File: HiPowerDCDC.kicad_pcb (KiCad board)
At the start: 2 copper layers, 111.2 x 100 mm, 61 parts, among them J1 Conn_01x01, J2 Conn_01x01, J3 Conn_01x01, J4 Conn_01x01, J5 Conn_01x04, Q1 WMJ38N60, Q2 WMJ38N60, SW1 SW_Push, SW2 SW_Push, U1 ESP32-WROOM-32U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

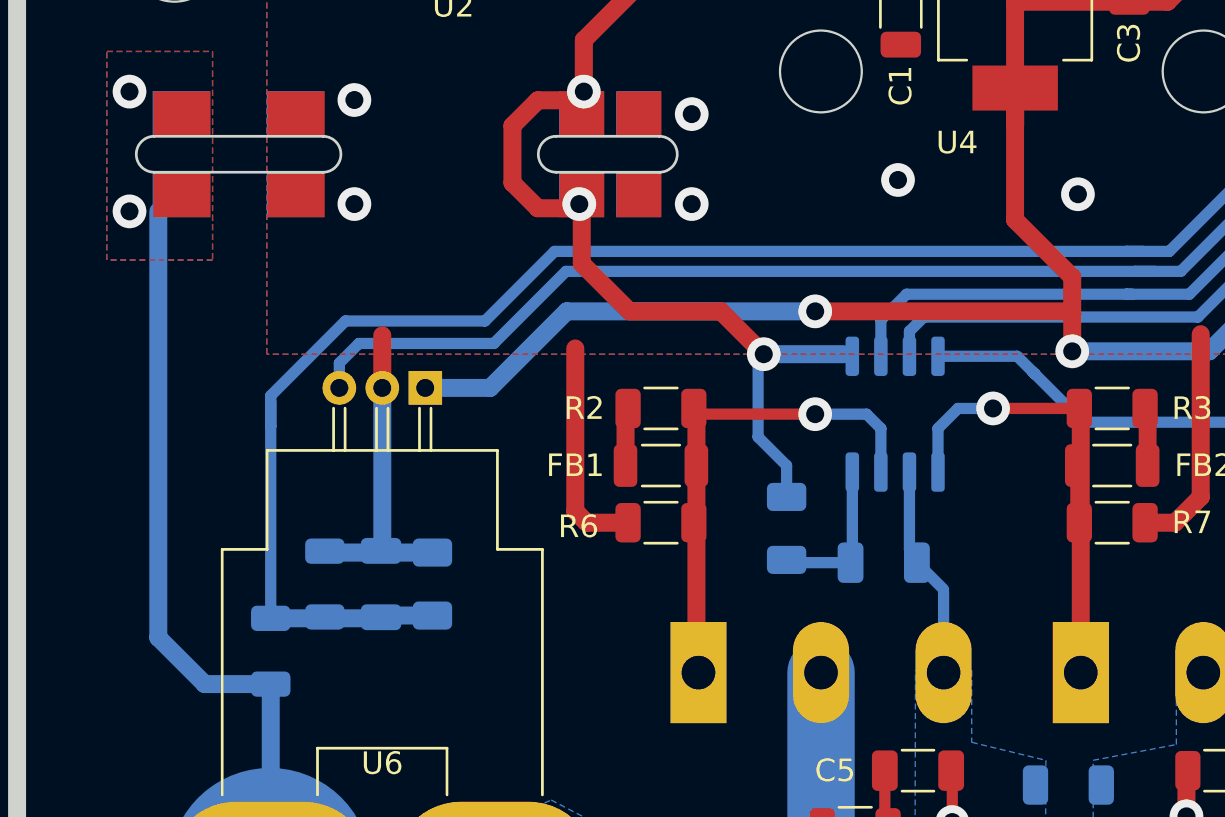
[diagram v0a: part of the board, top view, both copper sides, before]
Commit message: Changed FR107 footprint
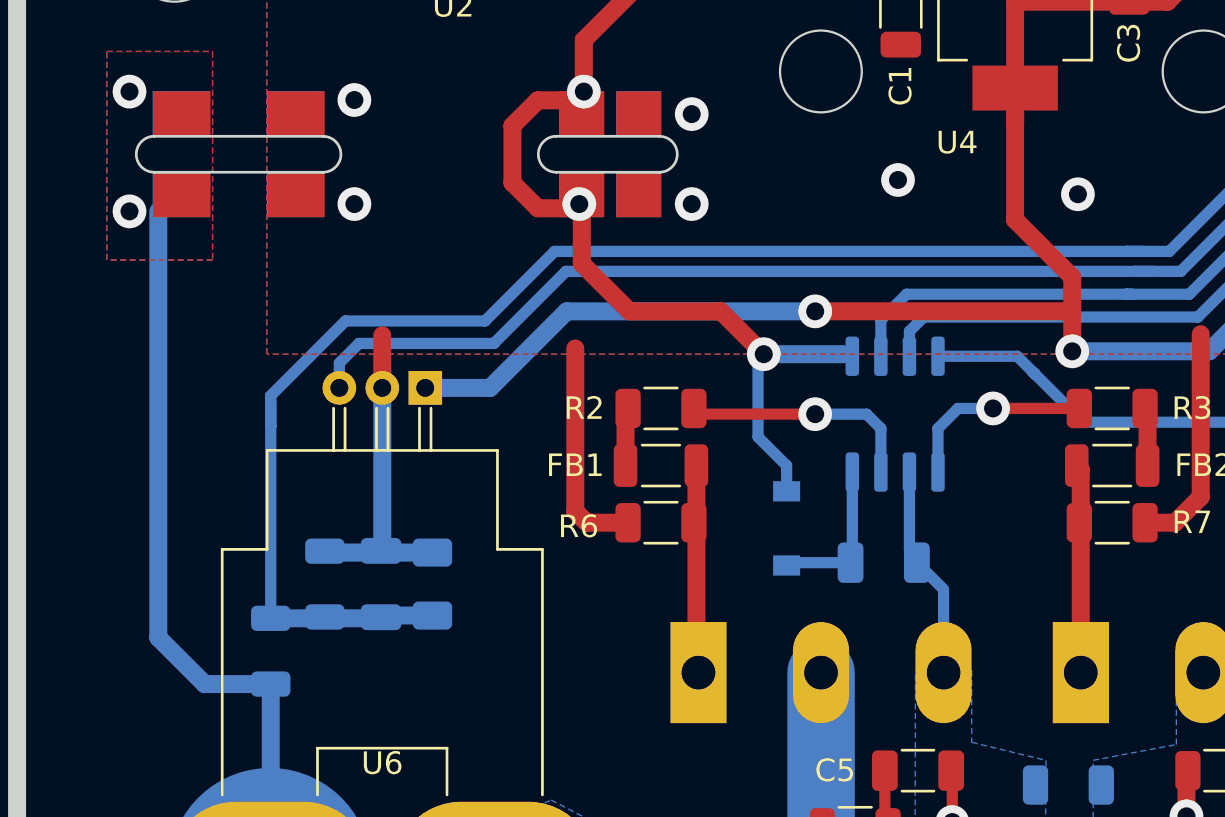
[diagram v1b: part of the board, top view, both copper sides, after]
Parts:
- D1: value D -> FR107; footprint Diode_SMD:D_1206_3216Metric -> Diode_SMD:D_SOD-123
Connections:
- R2 pad 1: Net-(FB1-Pad2) -> Net-(R2-Pad1)
- R3 pad 1: Net-(FB2-Pad2) -> Net-(R3-Pad1)
- U3 pad 5: Net-(FB2-Pad2) -> Net-(R3-Pad1)
- U3 pad 7: Net-(FB1-Pad2) -> Net-(R2-Pad1)
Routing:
- net Net-(FB2-Pad2): track 21.8 -> 9.37 mm, vias 1 -> 0
- net Net-(FB1-Pad2): track 19.8 -> 9.14 mm, vias 1 -> 0
- net Net-(R2-Pad1): track 0.00 -> 10.6 mm, vias 0 -> 1
- net Net-(R3-Pad1): track 0.00 -> 8.59 mm, vias 0 -> 1

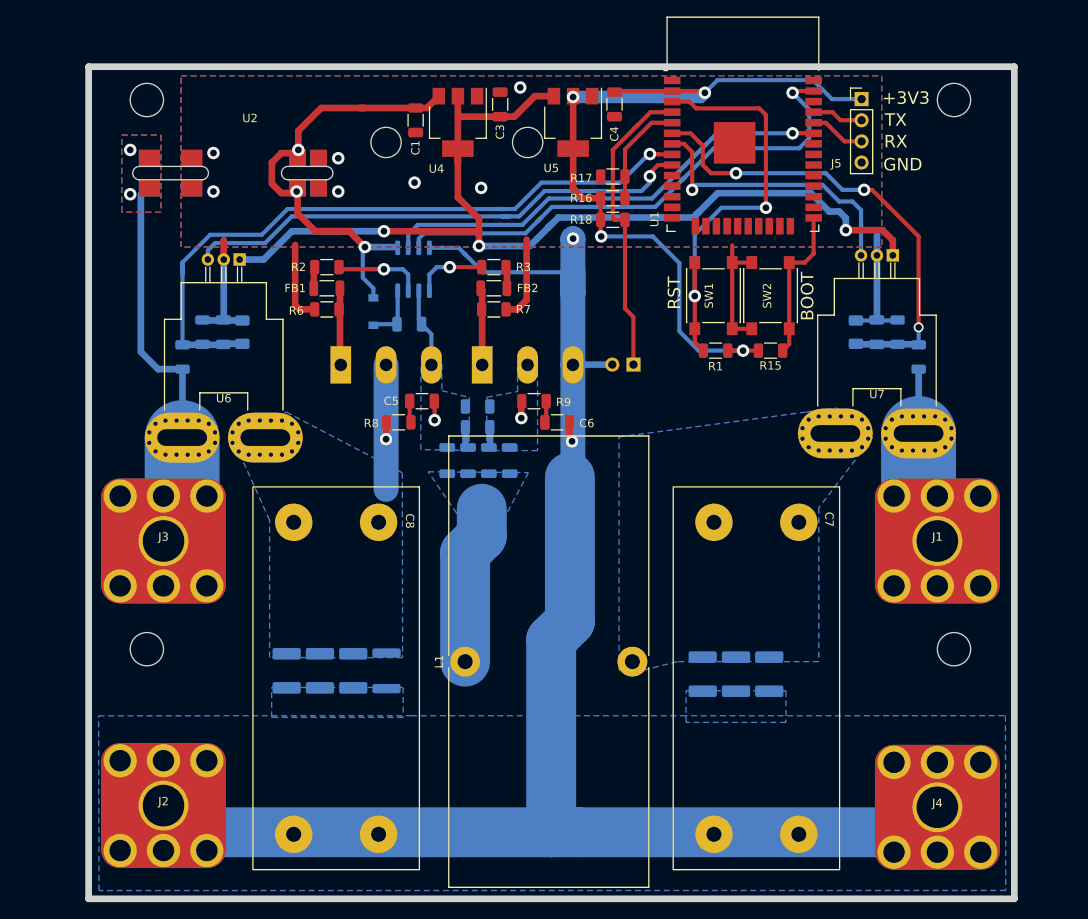
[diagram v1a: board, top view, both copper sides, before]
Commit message: Increased PCB width and made high P component more spaceous
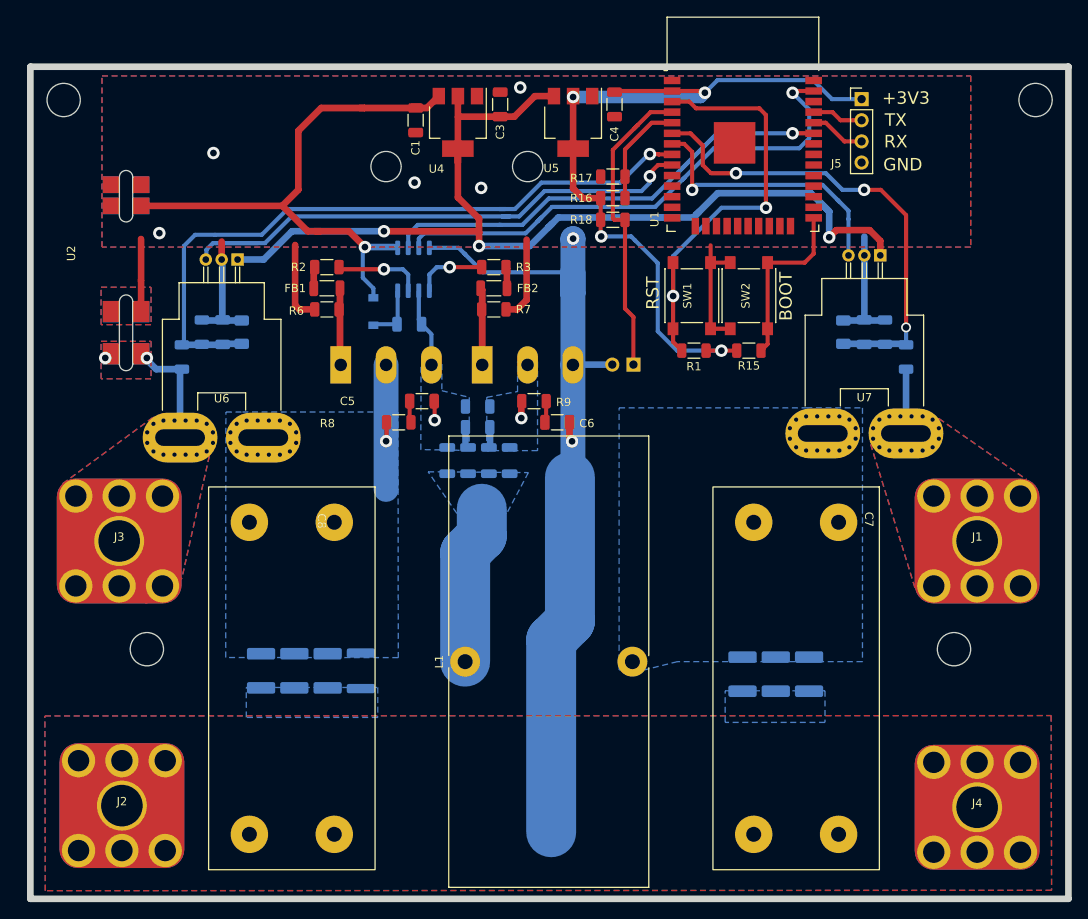
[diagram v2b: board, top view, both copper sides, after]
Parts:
- moved U2 17.7 mm to (111.2, 75.4), turned to -90 degrees
- moved C8 5.33 mm to (131.2, 126.5)
- moved J3 5.33 mm to (110.4, 110.0)
- moved J2 5.00 mm to (110.8, 141.8)
- moved C11 4.78 mm to (193.3, 126.0)
- moved C13 4.78 mm to (185.3, 126.0)
- moved C7 4.78 mm to (191.8, 126.5)
- moved C9 4.78 mm to (189.3, 126.0)
- moved J1 4.78 mm to (213.5, 110.0)
- moved J4 4.78 mm to (213.5, 142.0)
- moved C14 3.08 mm to (127.5, 125.6)
- moved C10 3.08 mm to (135.5, 125.6)
- moved C12 3.08 mm to (131.5, 125.6)
- moved R10 3.08 mm to (139.5, 125.6)
- moved SW1 2.60 mm to (179.2, 80.5)
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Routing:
- net GND: track 254.0 -> 173.4 mm, vias 9 -> 7
- net VDC: track 65.8 -> 14.0 mm
- net Net-(J1-Pad1): track 36.0 -> 12.9 mm
- net +12V: track 53.9 -> 68.5 mm, vias 3 -> 1
- net CIN: track 62.7 -> 68.1 mm
- net +3V3: track 98.2 -> 95.6 mm
- net Net-(R15-Pad1): track 18.6 -> 21.2 mm
- net COUT: track 35.7 -> 33.5 mm
- net +5V: track 123.1 -> 125.1 mm
- net Net-(R1-Pad1): track 51.4 -> 52.5 mm
- added copper zone on B.Cu, net Net-(J1-Pad1)
- added copper zone on F.Cu, net Net-(J1-Pad1)
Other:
- board size 111.2 x 100 mm -> 124.8 x 100 mm

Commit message: Added DCDC converter 12V->5V
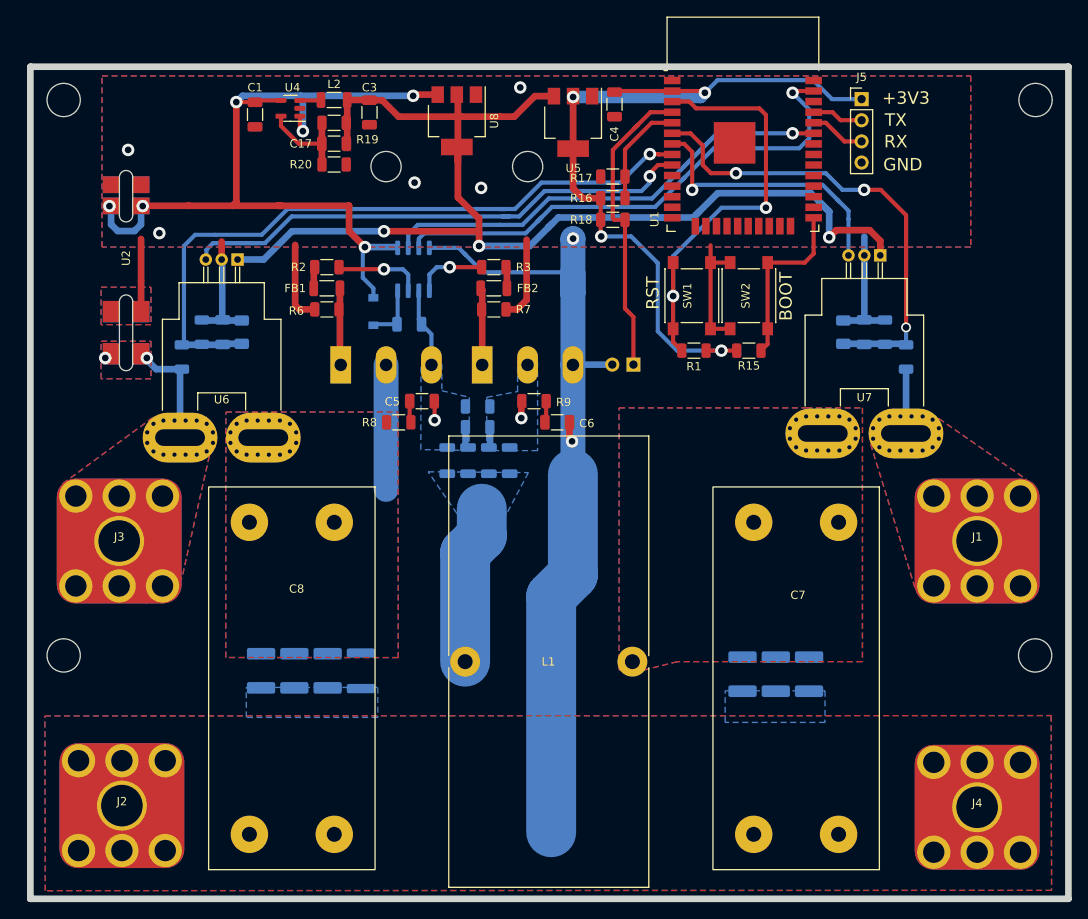
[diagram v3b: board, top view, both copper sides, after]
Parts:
- added C17: 22p, Capacitor_SMD:C_1206_3216Metric, F.Cu at (136.2, 62.2)
- added L2: 2u7, Inductor_SMD:L_1206_3216Metric, F.Cu at (136.2, 57.0)
- added R19: 4k7 1%, Resistor_SMD:R_1206_3216Metric, F.Cu at (136.2, 59.8)
- added R20: 1k 1%, Resistor_SMD:R_1206_3216Metric, F.Cu at (136.2, 64.8)
- added U8: AMS1117-5.0, Package_TO_SOT_SMD:SOT-223-3_TabPin2, F.Cu at (151.0, 59.5)
- C2: value 1u -> 10u
- U4: value AMS1117-5.0 -> XT3410; footprint Package_TO_SOT_SMD:SOT-223-3_TabPin2 -> Package_TO_SOT_SMD:SOT-23-5
- moved U4 20.2 mm to (131.0, 58.0), turned to 180 degrees
- moved C1 19.3 mm to (126.8, 58.8)
- moved C3 15.7 mm to (140.5, 58.5), turned to -90 degrees
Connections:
- U4 pad 1: GND -> +12V
- U4 pad 2: +5V -> GND
- U4 pad 3: +12V -> Net-(L2-Pad1)
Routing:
- net +12V: track 68.5 -> 99.0 mm, vias 1 -> 6
- net +5V: track 125.1 -> 144.9 mm
- net Net-(C17-Pad2): track 0.00 -> 12.0 mm
- net Net-(L2-Pad1): track 0.00 -> 2.56 mm
- net VCC: track 17.3 -> 15.0 mm, vias 1 -> 0
- added copper zone on F.Cu, net Net-(C11-Pad1)
- added copper zone on F.Cu, net VCC
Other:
- outline, holes or cut-outs redrawn

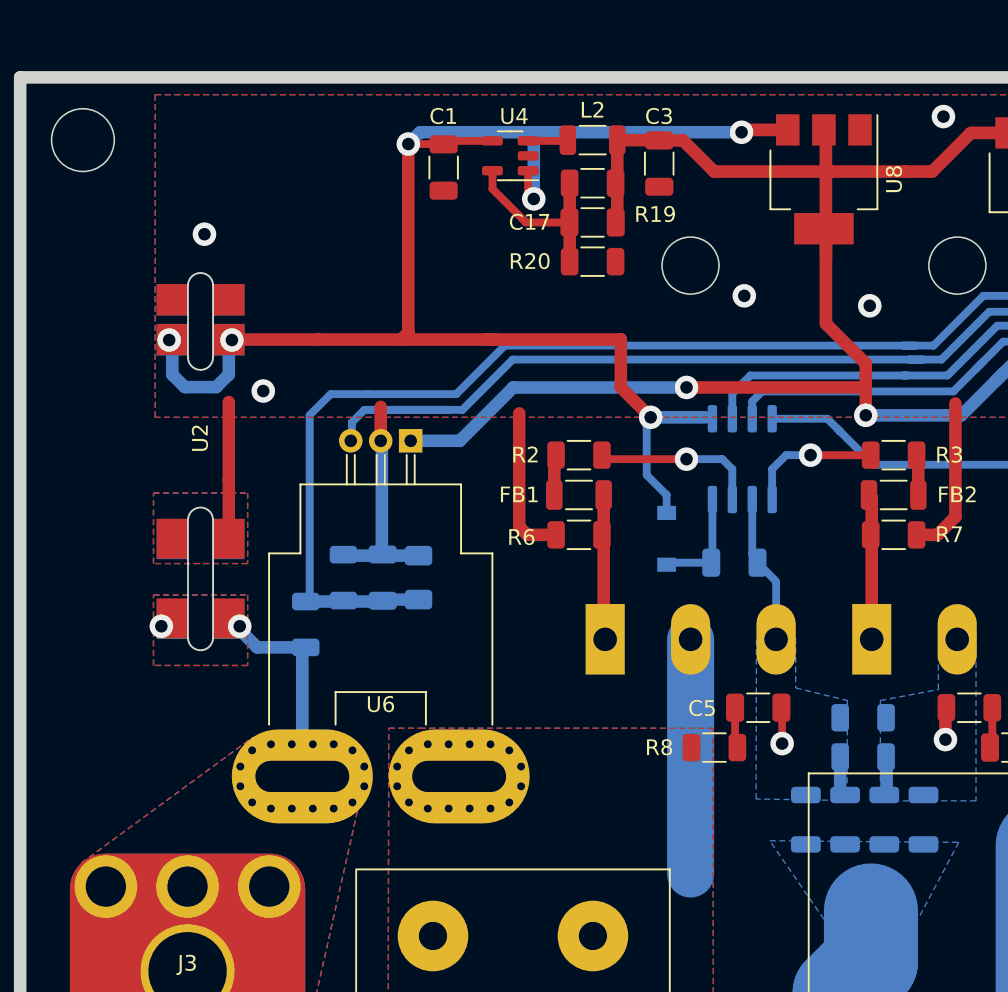
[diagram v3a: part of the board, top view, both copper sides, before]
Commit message: Changed ACDC converter to HLK-PM12
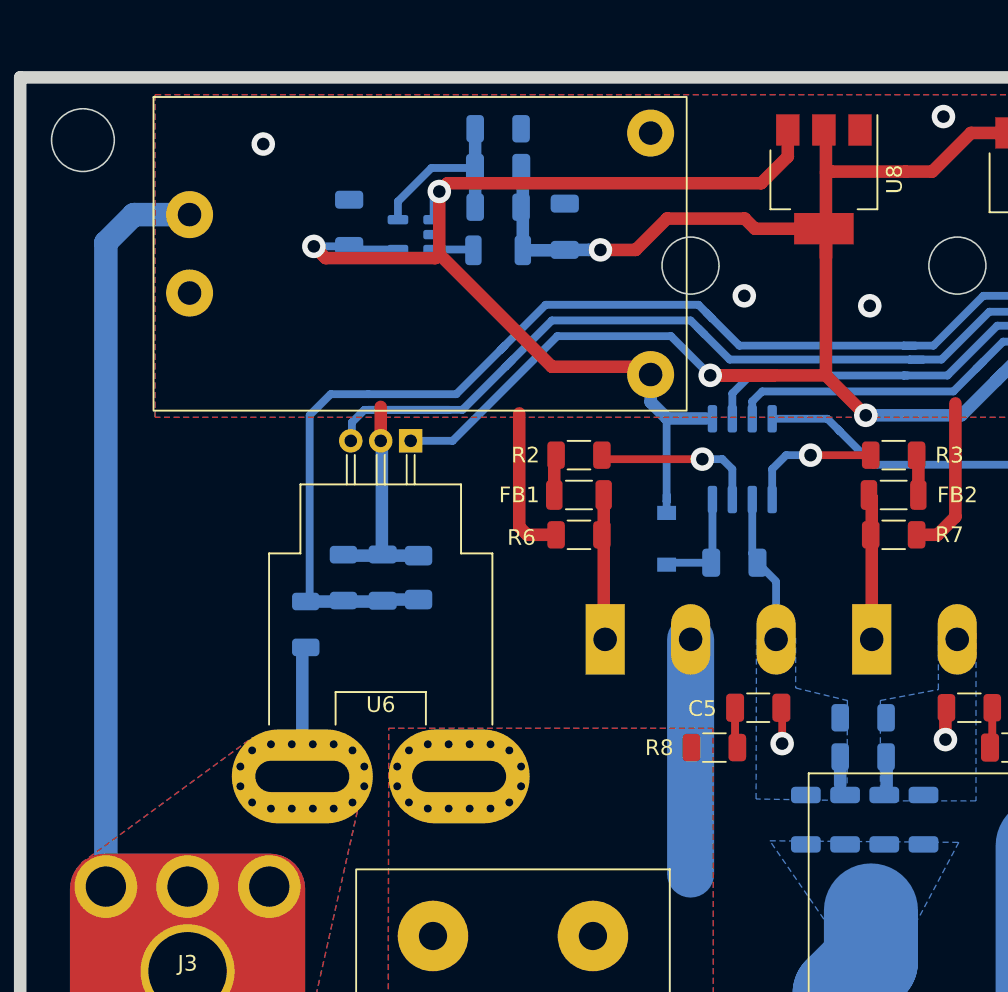
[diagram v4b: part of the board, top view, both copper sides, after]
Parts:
- C1, C17, C3, L2, R19, R20, U4: moved to B.Cu
- U2: footprint HiPowerFP:AC_DC_PCB_straight -> HiPowerFP:HLK-PM12
- moved U2 17.9 mm to (125.2, 64.2), turned to 0 degrees
- moved R20 10.4 mm to (130.2, 56.3)
- moved L2 9.25 mm to (130.2, 64.0)
- moved U4 7.85 mm to (125.0, 63.0)
- moved C3 7.25 mm to (134.5, 62.5), turned to 90 degrees
- moved C1 6.98 mm to (120.7, 62.3), turned to 90 degrees
- moved C17 6.96 mm to (130.2, 58.8)
- moved R19 6.22 mm to (130.2, 61.3)
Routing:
- net VDC: track 14.0 -> 55.5 mm, vias 2 -> 0
- net +12V: track 99.0 -> 73.3 mm, vias 6 -> 2
- net +5V: track 144.9 -> 154.6 mm, vias 3 -> 4
- net GND: track 173.4 -> 164.7 mm, vias 7 -> 6
- net CIN: track 68.1 -> 71.3 mm
- net VIN: track 82.5 -> 85.6 mm

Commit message: Finished PCB
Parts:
- L1: footprint Inductor_THT:L_Toroid_Vertical_L54.0mm_W23.8mm_P20.10mm_Bourns_5700 -> HiPowerFP:L_Toroid_Vertical_L54.0mm_W23.8mm_P20.10mm_Bourns_5700
- moved U2 1.50 mm to (123.8, 64.2)
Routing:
- net +5V: track 154.6 -> 135.9 mm
- net GND: track 164.7 -> 172.6 mm
- net +12V: track 73.3 -> 67.4 mm
- net VIN: track 85.6 -> 82.4 mm
- net CIN: track 71.3 -> 68.6 mm
- net VDC: track 55.5 -> 53.1 mm
- net Net-(U1-Pad33): track 62.2 -> 63.6 mm
- net Net-(U1-Pad37): track 63.0 -> 62.4 mm
- added copper zone on F.Cu, net +5V
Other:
- board size 124.8 x 100 mm -> 125.8 x 100 mm
